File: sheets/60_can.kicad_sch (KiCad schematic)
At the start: 17 parts, among them U1 ADM3055E

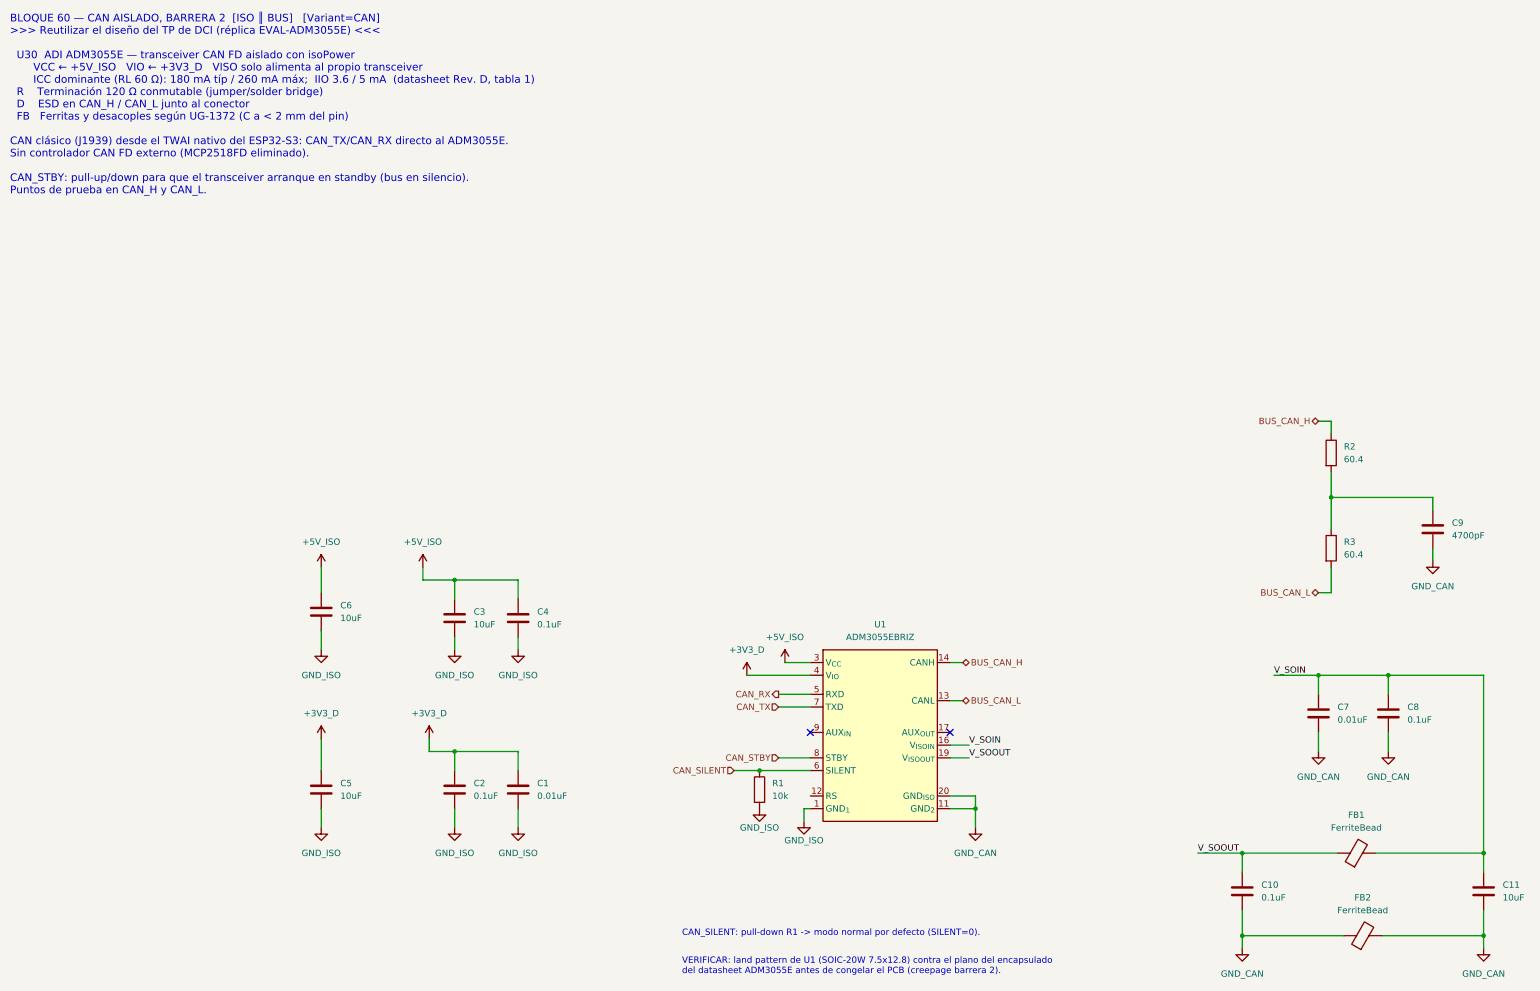
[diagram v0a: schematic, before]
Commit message: [Claude Code] 60_can, 70_output, 10_power_input: criterio prototipo = producción, campo DNP
- 60_can: ADM3055E según datasheet Rev. D (tabla 10): FB602 separa GNDISO
  de GND2, VISOOUT con 0.22 uF + 10 uF, RS a GND2 por R605 (0 ohm), AUXIN a
  GND1, pull-up de STBY, ESD2CAN24-Q1 DNP; referencias 6xx y campos completos.
- 70_output: DMN10H220LQ (100 V, SOT-23), SMAJ58A, buffer 74AHCT1G126
  (3.3 -> 5 V), zener de gate; latch y diagnóstico como huellas DNP.
- 10_power_input: J1/J2 MSTB 2,5 de 5.08 mm GF (J2 = 1776508), F101
  SF-2410FPA200W-2, C105 hold-up DNP; se quita un PWR_FLAG suelto en GND_CAN.
- Campo DNP (vacío / PROTO / PROD / PROTO,PROD) en todos los símbolos.
- README y PENDIENTES: decisiones del usuario, máximos de la entrada,
  temas abiertos (buck de la opción B, R109, TVS de entrada grande).

Co-Authored-By: Claude Opus 5.5 <noreply@anthropic.com>
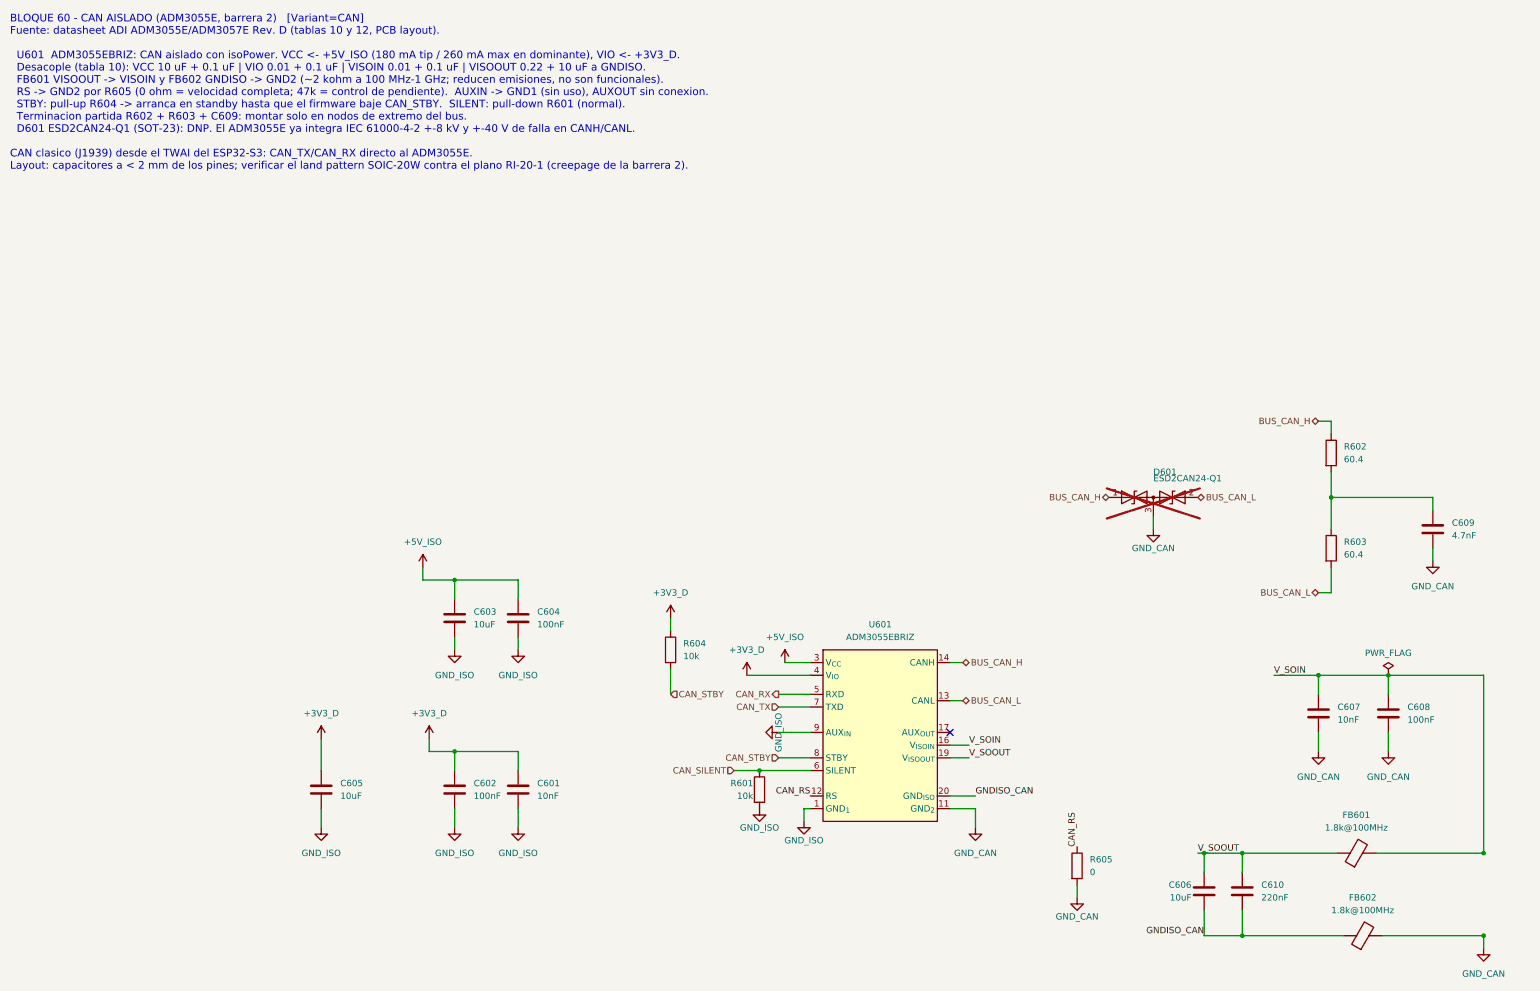
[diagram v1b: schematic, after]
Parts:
- removed C11, C6: 10uF, symbol Device:C
- added C606: 10uF, Capacitor_SMD:C_0805_2012Metric, symbol Device:C
- added D601: ESD2CAN24-Q1, Package_TO_SOT_SMD:SOT-23, symbol Device:D_TVS_Dual_AAC
- added R604: 10k, Resistor_SMD:R_0603_1608Metric, symbol Device:R
- added R605: 0, Resistor_SMD:R_0603_1608Metric, symbol Device:R
- C601: renamed from C1; value 0.01uF -> 10nF; footprint (none) -> Capacitor_SMD:C_0603_1608Metric; MPN (none) -> GCM188R71H103KA37D; Manufacturer (none) -> Murata; Notes (none) -> VIO: 0.01 uF + 0.1 uF (ADM3055E Rev. D, tabla 10). < 2 mm d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
- C602: renamed from C2; value 0.1uF -> 100nF; footprint (none) -> Capacitor_SMD:C_0603_1608Metric; MPN (none) -> GCM188R71H104KA57D; Manufacturer (none) -> Murata; Notes (none) -> VIO: 0.01 uF + 0.1 uF (ADM3055E Rev. D, tabla 10). < 2 mm d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
- C603: renamed from C3; footprint (none) -> Capacitor_SMD:C_0805_2012Metric; MPN (none) -> GCM21BR71A106KE22L; Manufacturer (none) -> Murata; Notes (none) -> VCC (isoPower): 10 uF + 0.1 uF (tabla 10). Picos de 180-260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
- C604: renamed from C4; value 0.1uF -> 100nF; footprint (none) -> Capacitor_SMD:C_0603_1608Metric; MPN (none) -> GCM188R71H104KA57D; Manufacturer (none) -> Murata; Notes (none) -> VCC: 10 uF + 0.1 uF (tabla 10). < 2 mm del pin.
- C605: renamed from C5; footprint (none) -> Capacitor_SMD:C_0805_2012Metric; MPN (none) -> GCM21BR71A106KE22L; Manufacturer (none) -> Murata; Notes (none) -> Reserva local de +3V3_D en VIO (no la exige el datasheet). 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
- C607: renamed from C7; value 0.01uF -> 10nF; footprint (none) -> Capacitor_SMD:C_0603_1608Metric; MPN (none) -> GCM188R71H103KA37D; Manufacturer (none) -> Murata; Notes (none) -> VISOIN: 0.01 uF + 0.1 uF a GND2 (tabla 10).
- C608: renamed from C8; value 0.1uF -> 100nF; footprint (none) -> Capacitor_SMD:C_0603_1608Metric; MPN (none) -> GCM188R71H104KA57D; Manufacturer (none) -> Murata; Notes (none) -> VISOIN: 0.01 uF + 0.1 uF a GND2 (tabla 10).
- C609: renamed from C9; value 4700pF -> 4.7nF; footprint (none) -> Capacitor_SMD:C_0603_1608Metric; MPN (none) -> GCM188R72A472KA37D; Manufacturer (none) -> Murata; Notes (none) -> Centro de la terminacion partida a GND_CAN. 100 V: el bus a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
- C610: renamed from C10; value 0.1uF -> 220nF; footprint (none) -> Capacitor_SMD:C_0603_1608Metric; MPN (none) -> GCM188R71E224KA55D; Manufacturer (none) -> Murata; Notes (none) -> VISOOUT: 0.22 uF + 10 uF a GNDISO (tabla 10).
- FB601: renamed from FB1; value FerriteBead -> 1.8k@100MHz; footprint (none) -> Inductor_SMD:L_0603_1608Metric; MPN (none) -> BLM18BD182SN1D; Manufacturer (none) -> Murata; Notes (none) -> VISOOUT -> VISOIN. ADI pide ~2 kohm entre 100 MHz y 1 GHz (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
- FB602: renamed from FB2; value FerriteBead -> 1.8k@100MHz; footprint (none) -> Inductor_SMD:L_0603_1608Metric; MPN (none) -> BLM18BD182SN1D; Manufacturer (none) -> Murata; Notes (none) -> GNDISO (pines 18/20) -> GND2. Una sola ferrita (Rev. D, tab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
- R601: renamed from R1; Notes (none) -> Pull-down de SILENT (el ADM3055E ya tiene pull-down interno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
- R602: renamed from R2; footprint (none) -> Resistor_SMD:R_0603_1608Metric; MPN (none) -> AC0603FR-0760R4L; Manufacturer (none) -> Yageo; Notes (none) -> Terminacion partida 2 x 60.4 ohm + C609. Montar solo en nod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
- R603: renamed from R3; footprint (none) -> Resistor_SMD:R_0603_1608Metric; MPN (none) -> AC0603FR-0760R4L; Manufacturer (none) -> Yageo; Notes (none) -> Terminacion partida 2 x 60.4 ohm + C609. Montar solo en nod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
- U601: renamed from U1; Notes (none) -> ADM3055E Rev. D: RS a GND2 por R605, AUXIN a GND1 (sin uso)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; Variant (none) -> CAN
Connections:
- net +3V3_D: now also R604.1
- net BUS_CAN_H: now also D601.1 (A1)
- net BUS_CAN_L: now also D601.2 (A2)
- net CAN_STBY: now also R604.2
- net GND_CAN: now also D601.3 (common), R605.2; no longer C610.2, FB602.1, U601.18 (GND_{ISO}), U601.20 (GND_{ISO})
- net GND_ISO: now also U601.9 (AUX_{IN})
- net V_SOOUT: now also C606.1
- net CAN_RS: now reaches U601.12 (RS)
- net CAN_RS: now also R605.1
- new net GNDISO_CAN: C606.2, C610.2, FB602.1, U601.18 (GND_{ISO}), U601.20 (GND_{ISO})
- no-connect marks 2 -> 1
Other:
- note added: "BLOQUE 60 - CAN AISLADO (ADM3055E, barrera 2) [Variant=CAN] Fuente: datasheet ADI ADM3055E/ADM3057E Rev. D (tablas 10 y 12, PCB layout). U601 ADM3055EBRIZ: CAN aislado con isoPower. VCC <- +5V_ISO (180 mA tip / 260 mA max en dominante), VIO <- +3V3_D. Desacople (tabla 10): VCC 10 uF + 0.1 uF | VIO 0.01 + 0.1 uF | VISOIN 0.01 + 0.1 uF | VISOOUT 0.22 + 10 uF a GNDISO. FB601 VISOOUT -> VISOIN y FB60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"
- note removed: "BLOQUE 60 — CAN AISLADO, BARRERA 2 [ISO ║ BUS] [Variant=CAN] >>> Reutilizar el diseño del TP de DCI (réplica EVAL-ADM3055E) <<< U30 ADI ADM3055E — transceiver CAN FD aislado con isoPower VCC ← +5V_ISO VIO ← +3V3_D VISO solo alimenta al propio transceiver ICC dominante (RL 60 Ω): 180 mA típ / 260 mA máx; IIO 3.6 / 5 mA (datasheet Rev. D, tabla 1) R Terminación 120 Ω conmutable (jumper/solder bridg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"
- note removed: "CAN_SILENT: pull-down R1 -> modo normal por defecto (SILENT=0)."
- note removed: "VERIFICAR: land pattern de U1 (SOIC-20W 7.5x12.8) contra el plano del encapsulado del datasheet ADM3055E antes de congelar el PCB (creepage barrera 2)."

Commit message: [Claude Code] 20_buck_5v: opción B (no aislada) con LMR38010; masas unificadas
- sheets/20_isolation -> sheets/20_buck_5v: se quitan PS201, ISO7763 y
  TPS7A1650; U201 LMR38010SQDDARQ1 (PROTO: LMR38010SDDAR, LCSC C5219310),
  5.02 V / 1 A a 400 kHz según TI SNVSC73B (L201 XAL6060-333, 3 x 22 uF,
  RT 64.9k, FB 100k/24.9k). Huella oficial HSOIC-8 con vías térmicas.
- Símbolo LMR38010 (easyeda2kicad) en lib/easyeda2kicad/INCLI-VA_easyeda,
  con tipos de pin ajustados; registrado en sym-lib-table.
- Todas las hojas: GND_ISO -> GND_VEH, +5V_ISO -> +5V_VEH.
- Raíz: EN/DIAG/FLT directos entre las hojas 40, 70 y 10; la hoja 20 sin pines.
- 10_power_input: R111 a +3V3_D, C109 = 100 nF (inrush con C105),
  C105 DNP solo en PROTO; se quita un PWR_FLAG suelto en GND_VEH.
- 70_output_ch: cambios de layout del usuario (hechos en KiCad).
- Textos de las hojas 30/40/50/80 y la raíz sin referencias al aislamiento.
- ERC: 0 en 10, 20, 30, 40, 50, 60 y 70; quedan los de 80 (hoja vacía).

Co-Authored-By: Claude Opus 5.5 <noreply@anthropic.com>
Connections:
- net +5V_ISO renamed +5V_VEH
- net GND_ISO renamed GND_VEH
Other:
- note added: "BLOQUE 60 - CAN AISLADO (ADM3055E, barrera 2) [Variant=CAN] Fuente: datasheet ADI ADM3055E/ADM3057E Rev. D (tablas 10 y 12, PCB layout). U601 ADM3055EBRIZ: CAN aislado con isoPower. VCC <- +5V_VEH (180 mA tip / 260 mA max en dominante), VIO <- +3V3_D. Desacople (tabla 10): VCC 10 uF + 0.1 uF | VIO 0.01 + 0.1 uF | VISOIN 0.01 + 0.1 uF | VISOOUT 0.22 + 10 uF a GNDISO. FB601 VISOOUT -> VISOIN y FB60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"
- note removed: "BLOQUE 60 - CAN AISLADO (ADM3055E, barrera 2) [Variant=CAN] Fuente: datasheet ADI ADM3055E/ADM3057E Rev. D (tablas 10 y 12, PCB layout). U601 ADM3055EBRIZ: CAN aislado con isoPower. VCC <- +5V_ISO (180 mA tip / 260 mA max en dominante), VIO <- +3V3_D. Desacople (tabla 10): VCC 10 uF + 0.1 uF | VIO 0.01 + 0.1 uF | VISOIN 0.01 + 0.1 uF | VISOOUT 0.22 + 10 uF a GNDISO. FB601 VISOOUT -> VISOIN y FB60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"
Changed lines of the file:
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@@
 	)
 	(symbol
-		(lib_id "INCLI-VA:GND_ISO")
+		(lib_id "INCLI-VA:GND_VEH")
 		(at 121.92 182.88 0)
 		(unit 1)
@@
 			)
 		)
-		(property "Value" "GND_ISO"
+		(property "Value" "GND_VEH"
 			(at 121.92 187.96 0)
 			(show_name no)
@@
 	)
 	(symbol
-		(lib_id "INCLI-VA:GND_ISO")
+		(lib_id "INCLI-VA:GND_VEH")
 		(at 170.18 179.07 0)
 		(unit 1)
@@
 			)
 		)
-		(property "Value" "GND_ISO"
+		(property "Value" "GND_VEH"
 			(at 170.18 182.88 0)
 			(show_name no)
@@
 	)
 	(symbol
-		(lib_id "INCLI-VA:GND_ISO")
+		(lib_id "INCLI-VA:GND_VEH")
 		(at 109.22 147.32 0)
 		(unit 1)
@@
 			)
 		)
-		(property "Value" "GND_ISO"
+		(property "Value" "GND_VEH"
 			(at 109.22 152.4 0)
 			(show_name no)
@@
 	)
 	(symbol
-		(lib_id "INCLI-VA:+5V_ISO")
+		(lib_id "INCLI-VA:+5V_VEH")
 		(at 102.87 130.81 0)
 		(unit 1)
@@
 			)
 		)
-		(property "Value" "+5V_ISO"
+		(property "Value" "+5V_VEH"
 			(at 102.87 125.73 0)
 			(show_name no)
@@
 	)
 	(symbol
-		(lib_id "INCLI-VA:GND_ISO")
+		(lib_id "INCLI-VA:GND_VEH")
 		(at 179.07 181.61 0)
 		(unit 1)
@@
 			)
 		)
-		(property "Value" "GND_ISO"
+		(property "Value" "GND_VEH"
 			(at 179.07 185.42 0)
 			(show_name no)
@@
 	)
 	(symbol
-		(lib_id "INCLI-VA:GND_ISO")
+		(lib_id "INCLI-VA:GND_VEH")
 		(at 121.92 147.32 0)
 		(unit 1)
@@
 			)
 		)
-		(property "Value" "GND_ISO"
+		(property "Value" "GND_VEH"
 			(at 121.92 152.4 0)
 			(show_name no)
@@
 	)
 	(symbol
-		(lib_id "INCLI-VA:+5V_ISO")
+		(lib_id "INCLI-VA:+5V_VEH")
 		(at 175.26 149.86 0)
 		(unit 1)
@@
 			)
 		)
-		(property "Value" "+5V_ISO"
+		(property "Value" "+5V_VEH"
 			(at 175.26 144.78 0)
 			(show_name no)
@@
 	)
 	(symbol
-		(lib_id "INCLI-VA:GND_ISO")
+		(lib_id "INCLI-VA:GND_VEH")
 		(at 109.22 182.88 0)
 		(unit 1)
@@
 			)
 		)
-		(property "Value" "GND_ISO"
+		(property "Value" "GND_VEH"
 			(at 109.22 187.96 0)
 			(show_name no)
@@
 	)
 	(symbol
-		(lib_id "INCLI-VA:GND_ISO")
+		(lib_id "INCLI-VA:GND_VEH")
 		(at 82.55 182.88 0)
 		(unit 1)
@@
 			)
 		)
-		(property "Value" "GND_ISO"
+		(property "Value" "GND_VEH"
 			(at 82.55 187.96 0)
 			(show_name no)
@@
 	)
 	(symbol
-		(lib_id "INCLI-VA:GND_ISO")
+		(lib_id "INCLI-VA:GND_VEH")
 		(at 173.99 163.83 270)
 		(unit 1)
@@
 			)
 		)
-		(property "Value" "GND_ISO"
+		(property "Value" "GND_VEH"
 			(at 173.99 163.83 0)
 			(show_name no)
@@
 		)
 	)
-	(text "BLOQUE 60 - CAN AISLADO (ADM3055E, barrera 2)   [Variant=CAN]\nFuente: datasheet ADI ADM3055E/ADM3057E Rev. D (tablas 10 y 12, PCB layout).\n\n  U601  ADM3055EBRIZ: CAN aislado con isoPower. VCC <- +5V_ISO (180 mA tip / 260 mA max en dominante), VIO <- +3V3_D.\n  Desacople (tabla 10): VCC 10 uF + 0.1 uF | VIO 0.01 + 0.1 uF | VISOIN 0.01 + 0.1 uF | VISOOUT 0.22 + 10 uF a GNDISO.\n  FB601 VISOOUT -> VISOIN y FB602 GNDISO -> GND2 (~2 kohm a 100 MHz-1 GHz; reducen emisiones, no son funcionales).\n  RS -> GND2 por R605 (0 ohm = velocidad completa; 47k = control de pendiente).  AUXIN -> GND1 (sin uso), AUXOUT sin conexion.\n  STBY: pull-up R604 -> arranca en standby hasta que el firmware baje CAN_STBY.  SILENT: pull-down R601 (normal).\n  Terminacion partida R602 + R603 + C609: montar solo en nodos de extremo del bus.\n  D601 ESD2CAN24-Q1 (SOT-23): DNP. El ADM3055E ya integra IEC 61000-4-2 +-8 kV y +-40 V de falla en CANH/CANL.\n\nCAN clasico (J1939) desde el TWAI del ESP32-S3: CAN_TX/CAN_RX directo al ADM3055E.\nLayout: capacitores a < 2 mm de los pines; verificar el land pattern SOIC-20W contra el plano RI-20-1 (creepage de la barrera 2)."
+	(text "BLOQUE 60 - CAN AISLADO (ADM3055E, barrera 2)   [Variant=CAN]\nFuente: datasheet ADI ADM3055E/ADM3057E Rev. D (tablas 10 y 12, PCB layout).\n\n  U601  ADM3055EBRIZ: CAN aislado con isoPower. VCC <- +5V_VEH (180 mA tip / 260 mA max en dominante), VIO <- +3V3_D.\n  Desacople (tabla 10): VCC 10 uF + 0.1 uF | VIO 0.01 + 0.1 uF | VISOIN 0.01 + 0.1 uF | VISOOUT 0.22 + 10 uF a GNDISO.\n  FB601 VISOOUT -> VISOIN y FB602 GNDISO -> GND2 (~2 kohm a 100 MHz-1 GHz; reducen emisiones, no son funcionales).\n  RS -> GND2 por R605 (0 ohm = velocidad completa; 47k = control de pendiente).  AUXIN -> GND1 (sin uso), AUXOUT sin conexion.\n  STBY: pull-up R604 -> arranca en standby hasta que el firmware baje CAN_STBY.  SILENT: pull-down R601 (normal).\n  Terminacion partida R602 + R603 + C609: montar solo en nodos de extremo del bus.\n  D601 ESD2CAN24-Q1 (SOT-23): DNP. El ADM3055E ya integra IEC 61000-4-2 +-8 kV y +-40 V de falla en CANH/CANL.\n\nCAN clasico (J1939) desde el TWAI del ESP32-S3: CAN_TX/CAN_RX directo al ADM3055E.\nLayout: capacitores a < 2 mm de los pines; verificar el land pattern SOIC-20W contra el plano RI-20-1 (creepage de la barrera 2)."
 		(exclude_from_sim no)
 		(at 20.32 20.32 0)
